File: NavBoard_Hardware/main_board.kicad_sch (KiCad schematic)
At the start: 10 parts, among them J1 24Pin To 16Pin, J2 24Pin to 16Pin, J3 Conn_02x03, J4 Ethernet Jack w/ Magnetics

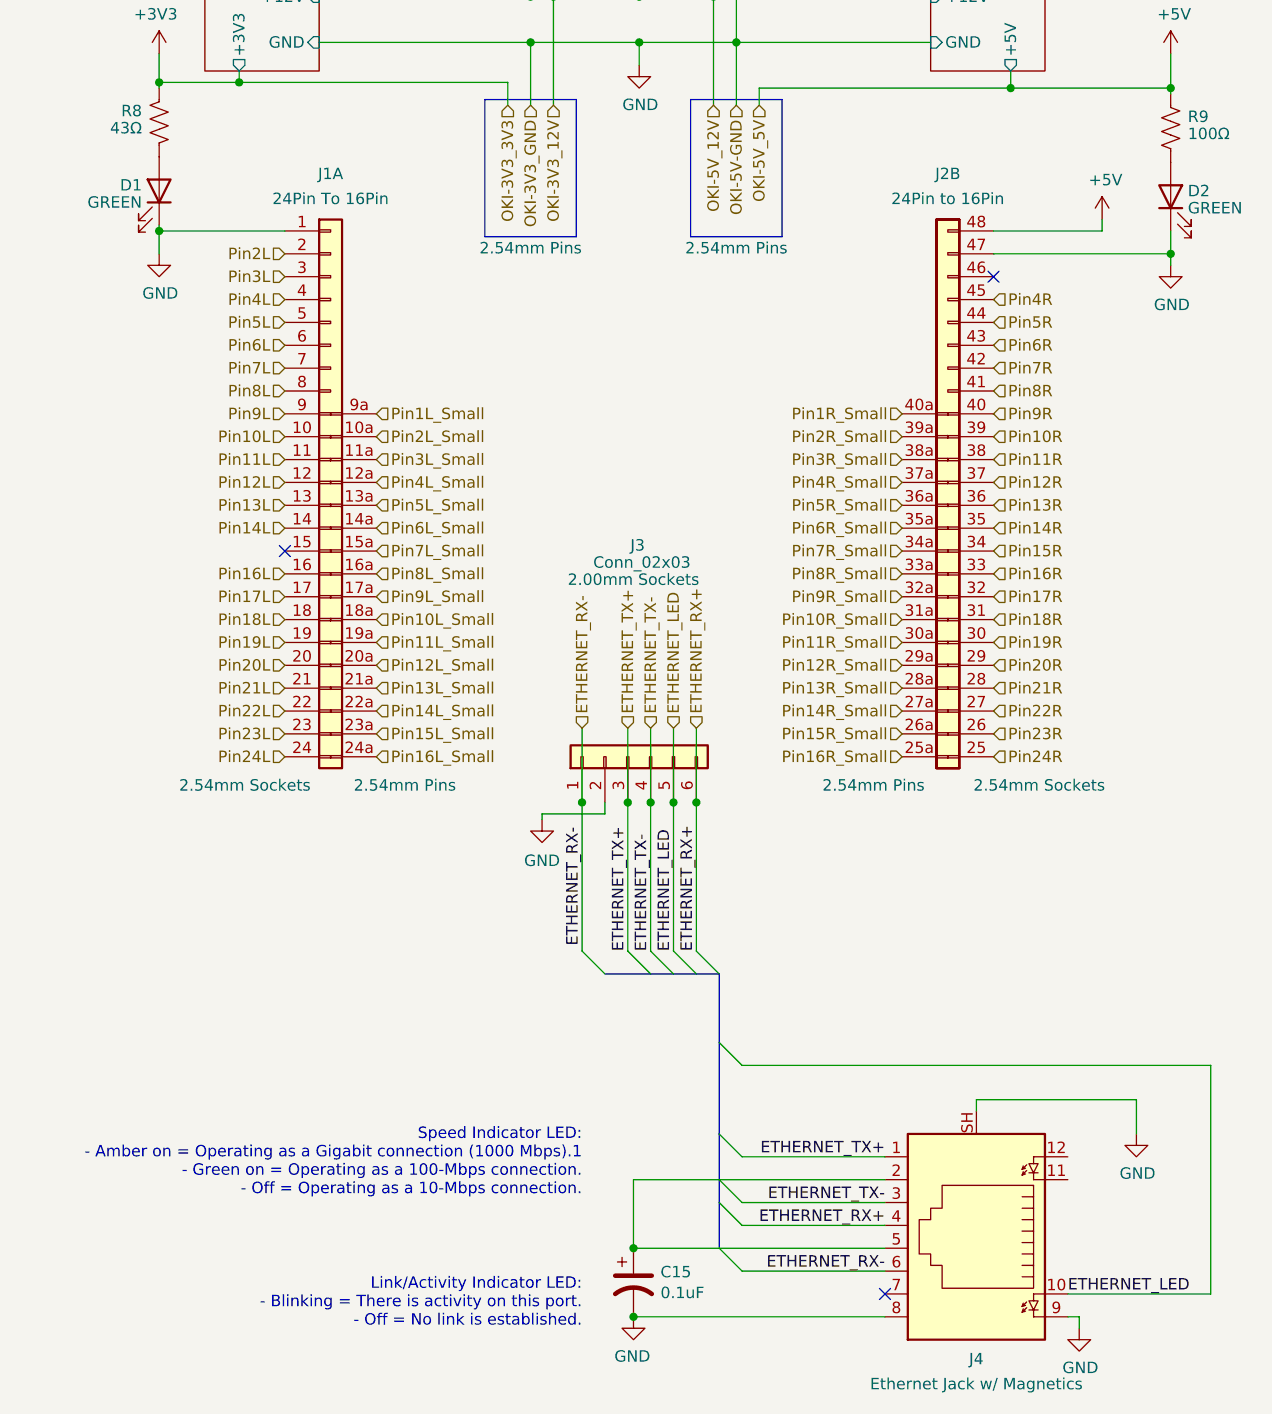
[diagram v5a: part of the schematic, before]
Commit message: Corrected pinout of RJ45 symbol, squashed some bugs
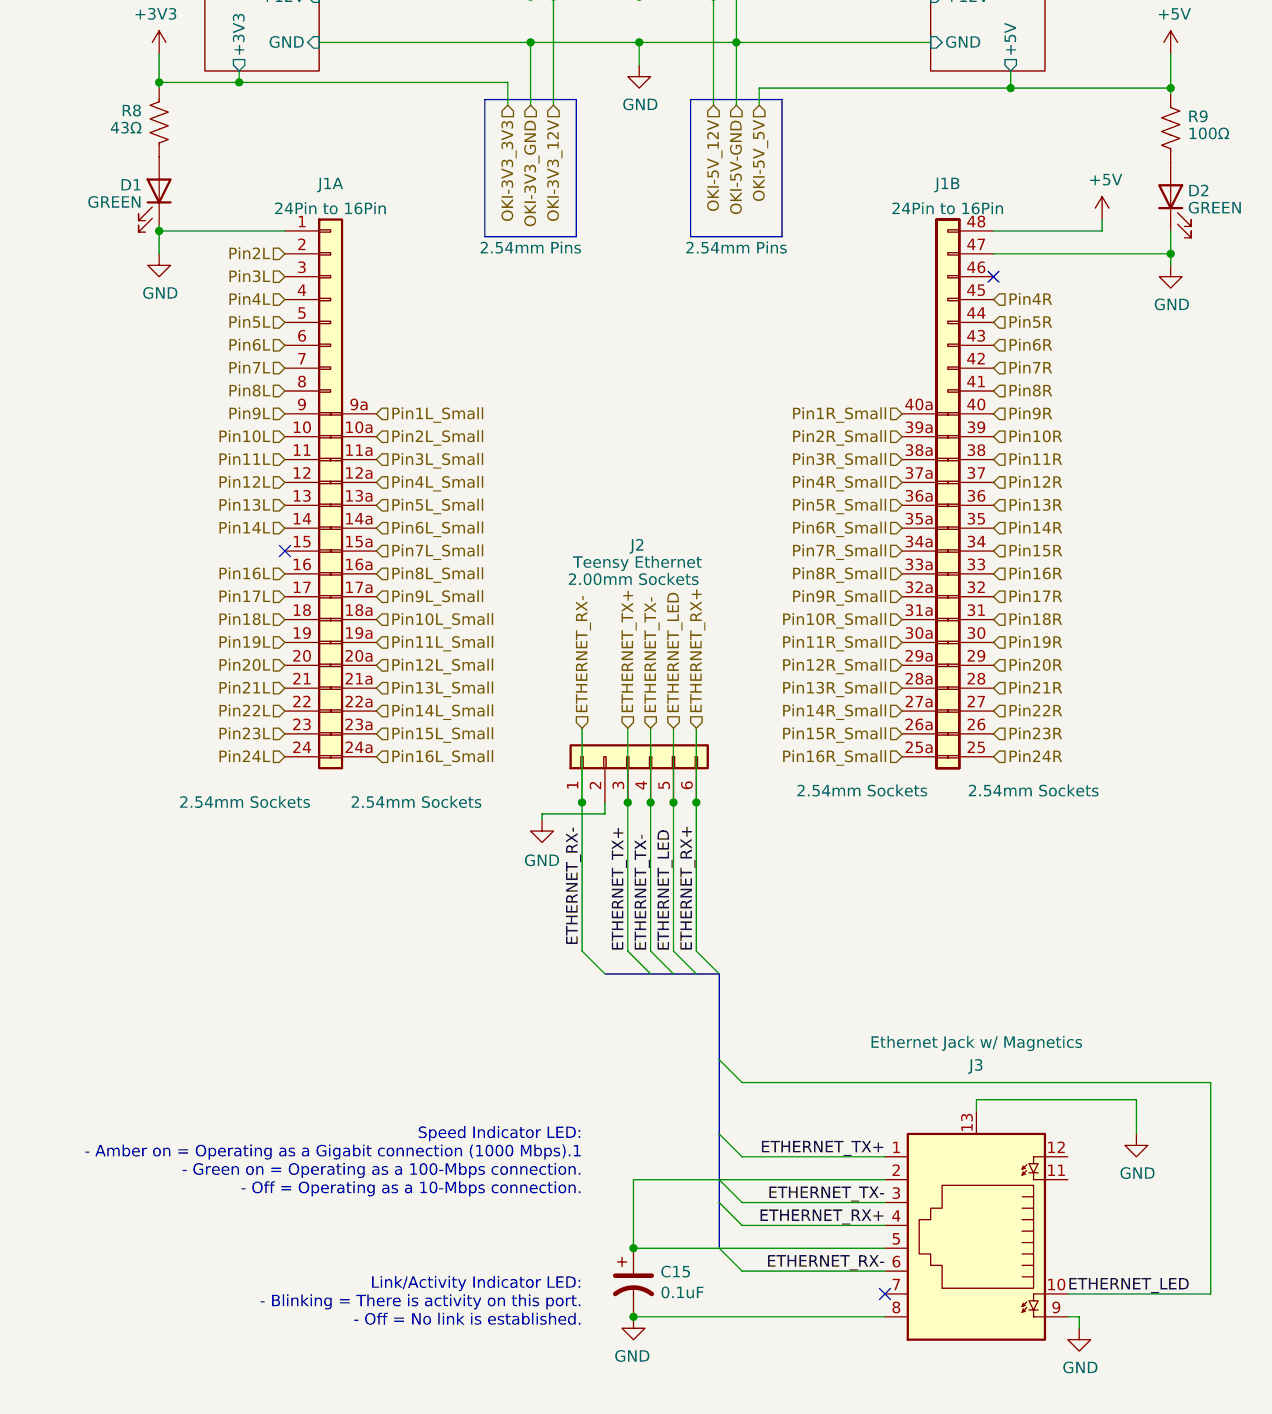
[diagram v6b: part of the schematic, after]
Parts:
- removed J2: 24Pin to 16Pin, Nav_Board:24Pin_To_16Pin_2.54mm_Separate_Pins, symbol Nav_Board:24Pin_To_16Pin_2.54mm_Separate_Pins_Alt
- added unit 2 of J1
- J1: value 24Pin To 16Pin -> 24Pin to 16Pin; 16Pin Type 2.54mm Pins -> (none); 24Pin Type 2.54mm Sockets -> (none); Field5 (none) -> 2.54mm Sockets; Inner Headers (none) -> 2.54mm Sockets
- J2: renamed from J3; value Conn_02x03 -> Teensy Ethernet
- renumbered J4 to J3
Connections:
- net +5V: now also J1.48
- net GND: now also J3.13, J1.47; no longer J3.SH
- net Pin10R: now also J1.39
- net Pin10R_Small: now also J1.31a
- net Pin11R: now also J1.38
- net Pin11R_Small: now also J1.30a
- net Pin12R: now also J1.37
- net Pin12R_Small: now also J1.29a
- net Pin13R: now also J1.36
- net Pin13R_Small: now also J1.28a
- net Pin14R: now also J1.35
- net Pin14R_Small: now also J1.27a
- net Pin15R: now also J1.34
- net Pin15R_Small: now also J1.26a
- net Pin16R: now also J1.33
- net Pin16R_Small: now also J1.25a
- net Pin17R: now also J1.32
- net Pin18R: now also J1.31
- net Pin19R: now also J1.30
- net Pin1R_Small: now also J1.40a
- net Pin20R: now also J1.29
- net Pin21R: now also J1.28
- net Pin22R: now also J1.27
- net Pin23R: now also J1.26
- net Pin24R: now also J1.25
- net Pin2R_Small: now also J1.39a
- net Pin3R_Small: now also J1.38a
- net Pin4R: now also J1.45
- net Pin4R_Small: now also J1.37a
- net Pin5R: now also J1.44
- net Pin5R_Small: now also J1.36a
- net Pin6R: now also J1.43
- net Pin6R_Small: now also J1.35a
- net Pin7R: now also J1.42
- net Pin7R_Small: now also J1.34a
- net Pin8R: now also J1.41
- net Pin8R_Small: now also J1.33a
- net Pin9R: now also J1.40
- net Pin9R_Small: now also J1.32a

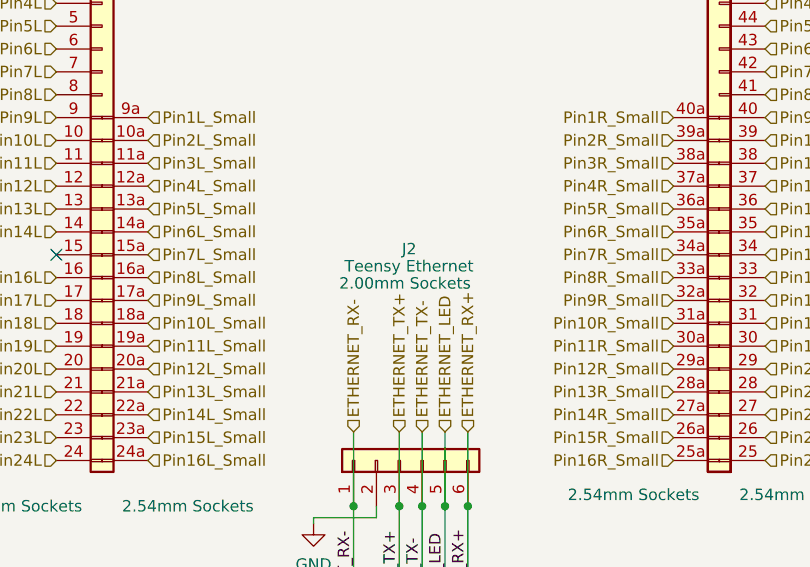
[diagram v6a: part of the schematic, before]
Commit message: Resized Ethernet to 2.54mm
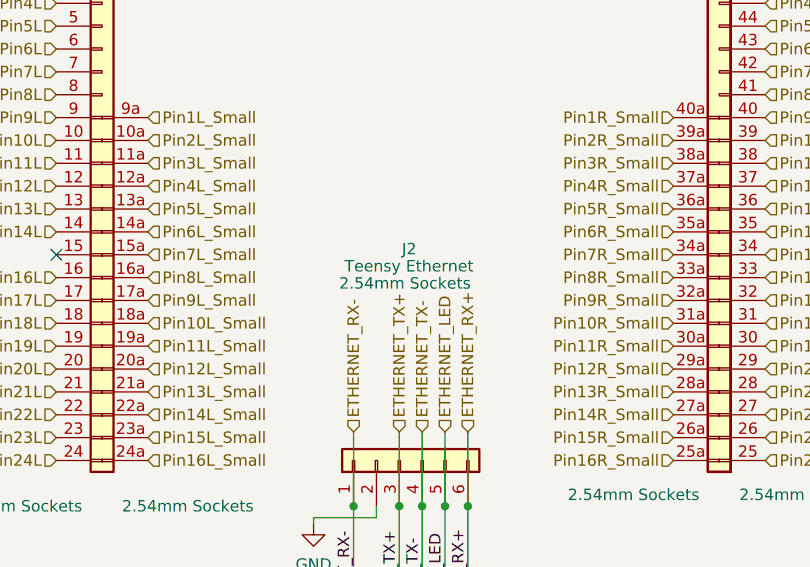
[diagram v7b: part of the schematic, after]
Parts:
- J2: footprint Connector_PinSocket_2.00mm:PinSocket_2x03_P2.00mm_Vertical -> Connector_PinSocket_2.54mm:PinSocket_2x03_P2.54mm_Vertical; Field4 2.00mm Sockets -> 2.54mm Sockets
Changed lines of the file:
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@@
       (effects (font (size 1.27 1.27)) (justify left))
     )
-    (property "Footprint" "Connector_PinSocket_2.00mm:PinSocket_2x03_P2.00mm_Vertical" (id 2) (at 92.075 121.92 0)
+    (property "Footprint" "Connector_PinSocket_2.54mm:PinSocket_2x03_P2.54mm_Vertical" (id 2) (at 92.075 121.92 0)
       (effects (font (size 1.27 1.27)) hide)
     )
@@
       (effects (font (size 1.27 1.27)) hide)
     )
-    (property "Field4" " 2.00mm Sockets" (id 4) (at 92.71 102.235 90))
+    (property "Field4" " 2.54mm Sockets" (id 4) (at 92.71 102.235 90))
     (pin "1")
     (pin "2")
